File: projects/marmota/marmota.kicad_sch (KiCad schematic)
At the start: 57 parts, among them J1 USB_C, J2 Conn_01x20_Pin, J3 Conn_01x20_Pin, SW1 Button top, SW2 Button side, U1 RP2040, U2 FLASH, U3 MCP73871, U4 RT6150B, U5 ESP32, Y1 12MHz

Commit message: Marmota RT6150 power save mode enabled, Replacement for crystal oscillator
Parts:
- Y1: LCSC C2149205 -> C2896601
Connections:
- net GND: now also U4.7 (PS)
- net VSYS: no longer U4.7 (PS)
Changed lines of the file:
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@@
 	)
 	(junction
+		(at 281.178 45.72)
+		(diameter 0)
+		(color 0 0 0 0)
+	)
+	(junction
 		(at 77.47 166.37)
 		(diameter 0)
@@
 	)
 	(junction
-		(at 270.002 38.1)
-		(diameter 0)
-		(color 0 0 0 0)
-	)
-	(junction
 		(at 270.002 30.48)
 		(diameter 0)
@@
 	(wire
 		(pts
-			(xy 270.002 45.72) (xy 292.1 45.72)
+			(xy 270.002 45.72) (xy 281.178 45.72)
 		)
 		(stroke
@@
 	(wire
 		(pts
+			(xy 281.178 45.72) (xy 292.1 45.72)
+		)
+		(stroke
+			(width 0)
+			(type default)
+		)
+	)
+	(wire
+		(pts
 			(xy 265.43 48.26) (xy 262.89 48.26)
 		)
@@
 	(wire
 		(pts
+			(xy 281.178 38.1) (xy 281.178 45.72)
+		)
+		(stroke
+			(width 0)
+			(type default)
+		)
+	)
+	(wire
+		(pts
 			(xy 261.62 120.65) (xy 264.16 120.65)
 		)
@@
 	(wire
 		(pts
-			(xy 270.002 38.1) (xy 285.75 38.1)
+			(xy 41.91 167.894) (xy 41.91 170.434)
 		)
 		(stroke
@@
 	(wire
 		(pts
-			(xy 41.91 167.894) (xy 41.91 170.434)
+			(xy 285.75 38.1) (xy 281.178 38.1)
 		)
 		(stroke
@@
 			)
 		)
-		(property "LCSC" "C2149205"
+		(property "LCSC" "C2896601"
 			(at 170.18 119.38 0)
 			(effects

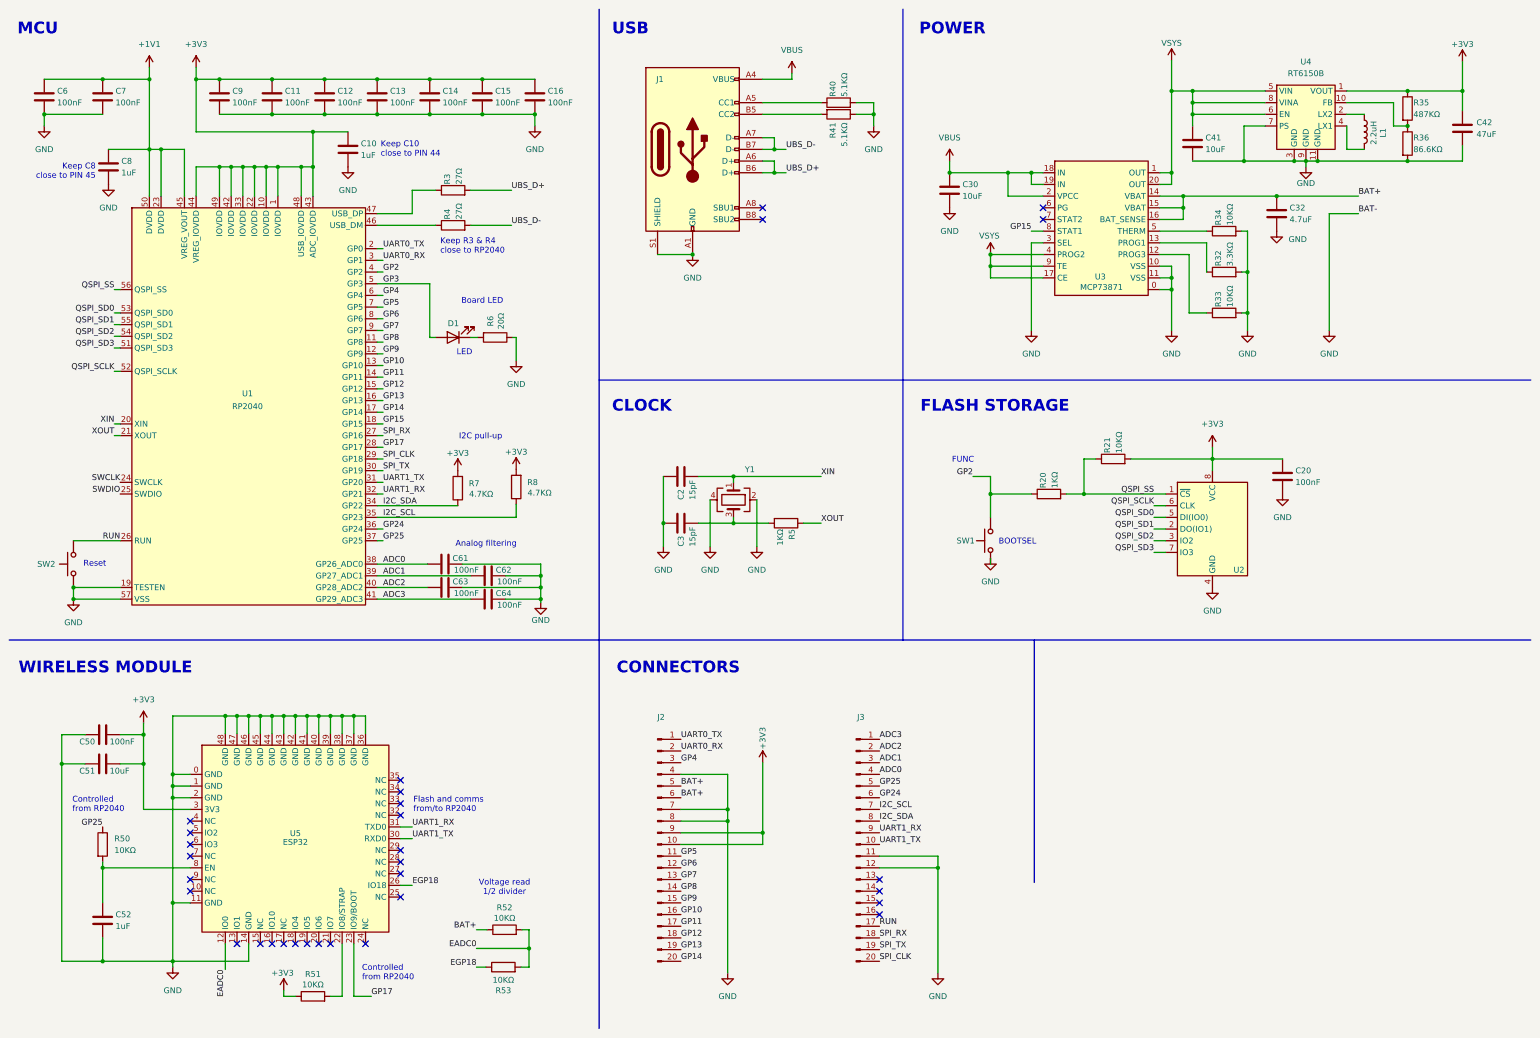
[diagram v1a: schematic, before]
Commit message: Connected RT buckboost power save pin to gpio, Shifted GPIOs
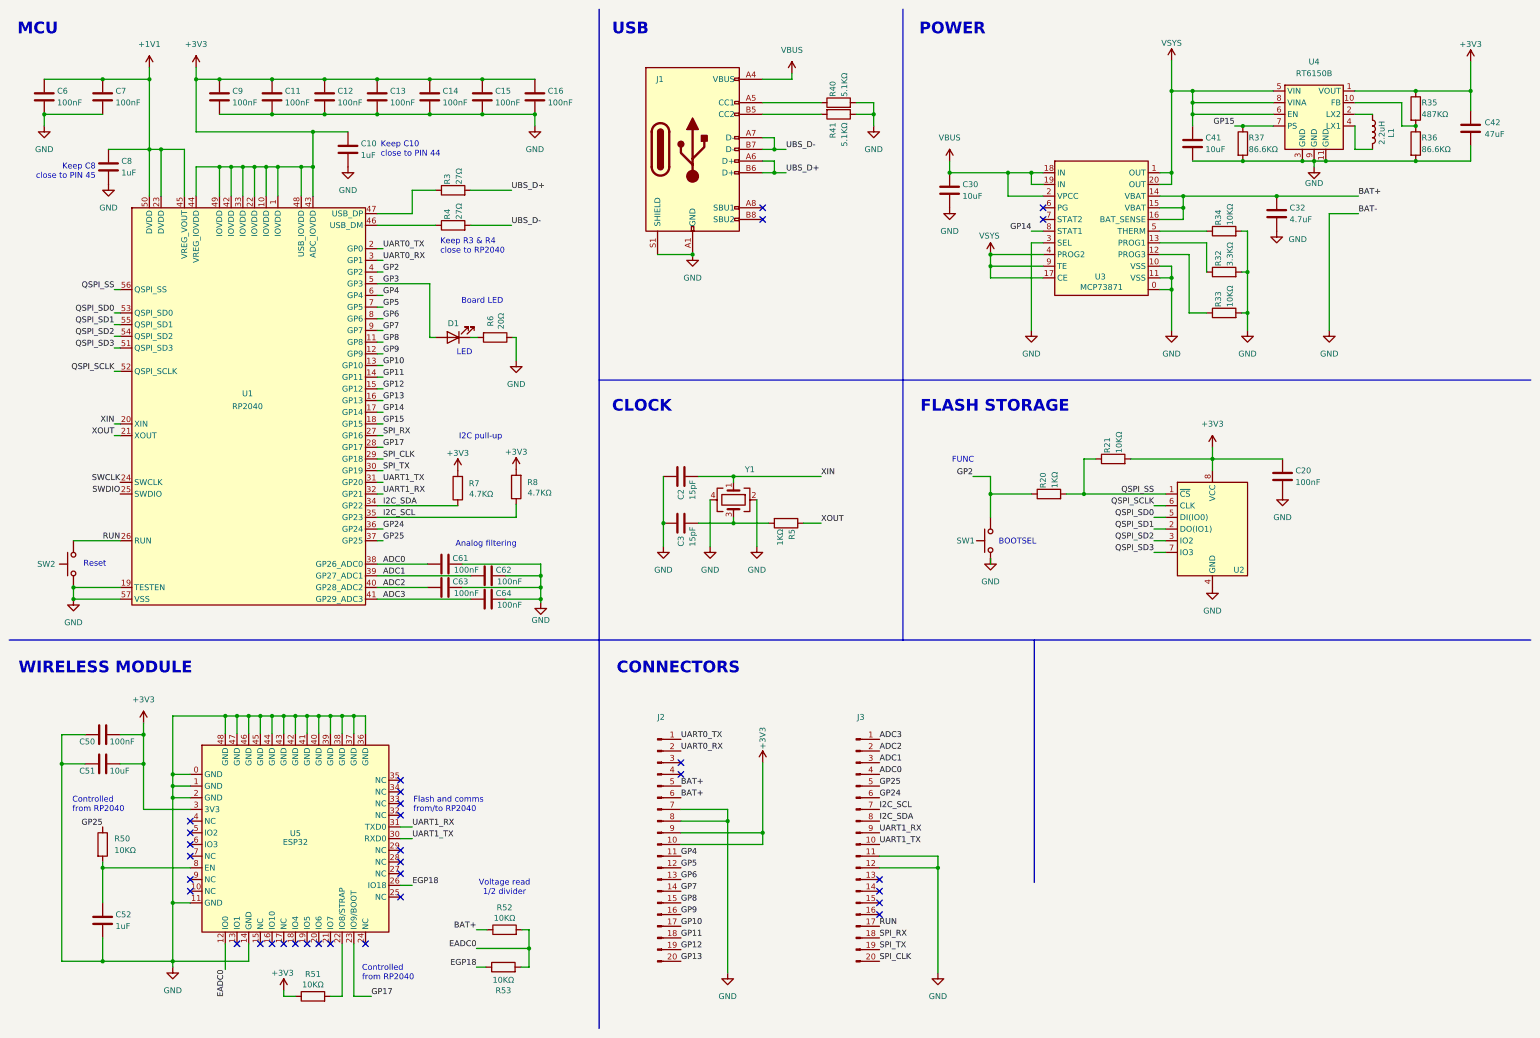
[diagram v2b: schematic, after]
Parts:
- added R37: 86.6KΩ, ILO_fp:0402_compact, symbol Device:R
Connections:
- net GND: now also R37.2; no longer J2.4 (Pin_4), U4.7 (PS)
- net GP10: now also J2.17 (Pin_17); no longer J2.16 (Pin_16)
- net GP11: now also J2.18 (Pin_18); no longer J2.17 (Pin_17)
- net GP12: now also J2.19 (Pin_19); no longer J2.18 (Pin_18)
- net GP13: now also J2.20 (Pin_20); no longer J2.19 (Pin_19)
- net GP14: now also U3.8 (STAT1); no longer J2.20 (Pin_20)
- net GP15: now also U4.7 (PS), R37.1; no longer U3.8 (STAT1)
- net GP4: now also J2.11 (Pin_11); no longer J2.3 (Pin_3)
- net GP5: now also J2.12 (Pin_12); no longer J2.11 (Pin_11)
- net GP6: now also J2.13 (Pin_13); no longer J2.12 (Pin_12)
- net GP7: now also J2.14 (Pin_14); no longer J2.13 (Pin_13)
- net GP8: now also J2.15 (Pin_15); no longer J2.14 (Pin_14)
- net GP9: now also J2.16 (Pin_16); no longer J2.15 (Pin_15)
- no-connect marks 31 -> 33
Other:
- moved on the sheet: C42, L1, R35, R36, U4

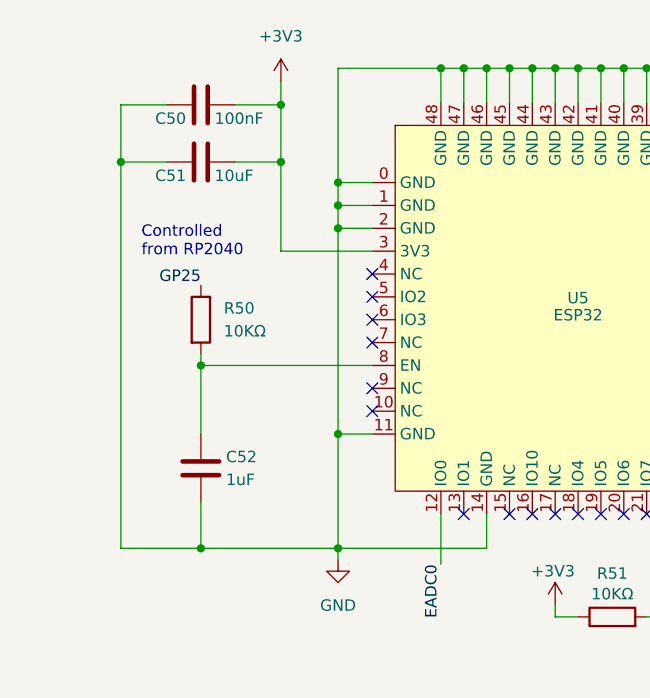
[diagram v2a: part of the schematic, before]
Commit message: Marmota ESP EN weak pull down
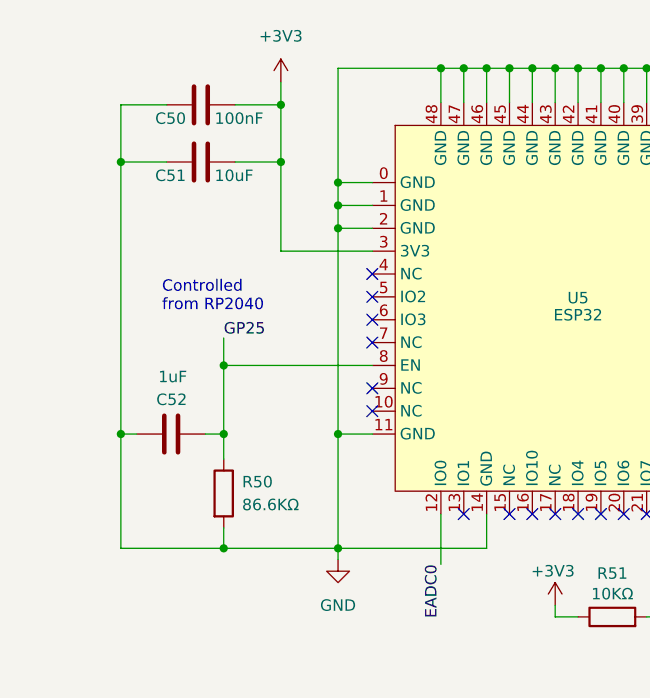
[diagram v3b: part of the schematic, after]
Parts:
- R50: value 10KΩ -> 86.6KΩ; LCSC C25744 -> C19709
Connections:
- net GND: now also C52.2, R50.2; no longer C52.1
- net GP25: now also C52.1, U5.8 (EN)
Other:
- moved on the sheet: C52
